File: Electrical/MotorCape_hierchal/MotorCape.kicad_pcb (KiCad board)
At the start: 2 copper layers, 24 parts, among them J1 FL, J10 T_SIG, J11 flag_wheel servo, J12 T_DB, J13 FR, J14 RightMotorController_PWR, J16 R_SIG, J17 BR, J2 LeftMotorController_PWR, J4 L_SIG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

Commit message: trying to lay-out things. lots of via's, this could be a bit messy
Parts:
- B1: value Front_Shifter -> SPARKFUN_LOGIC_LEVEL_CONVERTER
- B2: value Top_Shifter -> SPARKFUN_LOGIC_LEVEL_CONVERTER
- B3: value Right_Shifter -> SPARKFUN_LOGIC_LEVEL_CONVERTER
- J1: value FL -> Motor1
- J10: value T_SIG -> DualMotorController_SIG
- J12: value T_DB -> Motor2
- J13: value FR -> Motor1
- J14: value RightMotorController_PWR -> DualMotorController_PWR
- J16: value R_SIG -> DualMotorController_SIG
- J17: value BR -> Motor2
- J2: value LeftMotorController_PWR -> DualMotorController_PWR
- J4: value L_SIG -> DualMotorController_SIG
- J5: value BL -> Motor2
- J6: value T_FW -> Motor1
- J8: value TopMotorController_PWR -> DualMotorController_PWR
- P13: value batt_conn -> battery_connector
- moved J6 52.4 mm to (120.7, 88.3), turned to 180 degrees
- moved F1 37.8 mm to (123.9, 106.0)
- moved J12 33.3 mm to (119.6, 120.8), turned to 180 degrees
- moved U1 31.4 mm to (149.9, 101.0), turned to 180 degrees
- moved P13 29.2 mm to (70.5, 116.8), turned to 90 degrees
- moved P14 17.1 mm to (126.4, 101.6), turned to 180 degrees
- moved J14 16.2 mm to (83.2, 98.4)
- moved J2 15.0 mm to (108.6, 92.1)
- moved R1 12.5 mm to (144.2, 87.3), turned to 90 degrees
- moved J8 11.4 mm to (75.6, 72.4)
- moved R2 10.5 mm to (136.5, 84.5)
- moved J13 2.54 mm to (154.9, 108.0)
- moved J17 2.54 mm to (172.7, 108.6)
- moved J16 1.91 mm to (184.8, 114.3)
- moved J10 1.69 mm to (138.0, 110.7)
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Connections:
- J1 pad 2: Net-(J1-Pad2) -> MOTOR_GND
- J12 pad 2: Net-(J12-Pad2) -> MOTOR_GND
- J13 pad 2: Net-(J13-Pad2) -> MOTOR_GND
- J14 pad 1: Net-(J13-Pad2) -> MOTOR_GND
- J14 pad 6: Net-(J14-Pad6) -> MOTOR_GND
- J17 pad 2: Net-(J14-Pad6) -> MOTOR_GND
- J2 pad 1: Net-(J1-Pad2) -> MOTOR_GND
- J2 pad 6: Net-(J2-Pad6) -> MOTOR_GND
- J5 pad 2: Net-(J2-Pad6) -> MOTOR_GND
- J6 pad 2: Net-(J6-Pad2) -> MOTOR_GND
- J8 pad 1: Net-(J6-Pad2) -> MOTOR_GND
- J8 pad 6: Net-(J12-Pad2) -> MOTOR_GND
- R1 pad 2: Net-(R1-Pad2) -> +3V3
- R2 pad 1: SCL -> +3V3
- R2 pad 2: Net-(R2-Pad2) -> SCL
- U1 pad 12: Net-(R1-Pad2) -> SDA
- U1 pad 13: Net-(R2-Pad2) -> SCL
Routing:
- net +5V: track 0.00 -> 277.0 mm, vias 0 -> 2
- net Net-(J13-Pad1): track 0.00 -> 125.7 mm
- net +12V: track 0.00 -> 116.4 mm
- net Net-(J2-Pad5): track 0.00 -> 103.2 mm
- net Tx_To_Pi: track 0.00 -> 87.7 mm
- net Rx_From_Pi: track 0.00 -> 86.1 mm, vias 0 -> 1
- net MOTOR_PWR: track 0.00 -> 83.6 mm
- net +3V3: track 0.00 -> 77.9 mm, vias 0 -> 2
- net Net-(J14-Pad5): track 0.00 -> 74.4 mm
- net Net-(J1-Pad1): track 0.00 -> 67.9 mm
- net Net-(J12-Pad1): track 0.00 -> 54.2 mm
- net MOTOR_GND: track 0.00 -> 3.02 mm
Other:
- net class ArduinoSignals added: clearance 0.381, trace_width 0.381, via_dia 0.6858, via_drill 0.3302
- net class Default: clearance 0.2 -> 0.1524; trace_width 0.25 -> 0.1524; via_dia 0.6 -> 0.6858; via_drill 0.4 -> 0.3302
- net class IndvMotor added: clearance 1.016, trace_width 1.016, via_dia 0.6858, via_drill 0.3302
- net class MotorPower added: clearance 0.508, trace_width 2.032, via_dia 0.6858, via_drill 0.3302
- net class Signal added: clearance 0.381, trace_width 0.381, via_dia 0.6858, via_drill 0.3302
- net class SmallPower added: clearance 0.762, trace_width 0.762, via_dia 0.6858, via_drill 0.3302
- rule trace_clearance: 0.2 -> 0.1524
- rule trace_min: 0.2 -> 0.1524
- rule via_min_drill: 0.3 -> 0.3302
- rule via_min_size: 0.4 -> 0.6858
- board text added: "FR"
- board text added: "I2C"
- board text added: "Left"
- board text added: "Right"
- board text added: "Top"

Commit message: pushing changes while routing. still not done yet
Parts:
- moved J16 0.84 mm to (183.9, 114.2)
- moved B1 0.63 mm to (192.4, 111.8)
- moved B2 0.63 mm to (192.4, 97.8)
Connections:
- ARD1 pad 54: FrontLeft_ENC_A -> Net-(ARD1-Pad54)
- ARD1 pad 55: FrontLeft_ENC_B -> FrontLeft_ENC_A
- ARD1 pad 56: BackLeft_DIR -> Net-(ARD1-Pad56)
- ARD1 pad 57: BackLeft_ENC_A -> FrontLeft_ENC_B
- ARD1 pad 58: BackLeft_ENC_B -> Net-(ARD1-Pad58)
- ARD1 pad 59: FrontRight_DIR -> BackLeft_DIR
- ARD1 pad 60: FrontRight_ENC_A -> Net-(ARD1-Pad60)
- ARD1 pad 61: FrontRight_ENC_B -> BackLeft_ENC_A
- ARD1 pad 62: BackRight_DIR -> Net-(ARD1-Pad62)
- ARD1 pad 63: BackRight_ENC_A -> BackLeft_ENC_B
- ARD1 pad 64: BackRight_ENC_B -> Net-(ARD1-Pad64)
- ARD1 pad 65: FlagWheel_DIR -> FrontRight_DIR
- ARD1 pad 66: FlagWheel_ENC_A -> Net-(ARD1-Pad66)
- ARD1 pad 67: FlagWheel_ENC_B -> FrontRight_ENC_A
- ARD1 pad 68: DrawBridge_DIR -> Net-(ARD1-Pad68)
- ARD1 pad 69: DrawBridge_ENC_A -> FrontRight_ENC_B
- ARD1 pad 70: DrawBridge_ENC_B -> Net-(ARD1-Pad70)
- ARD1 pad 71: Net-(ARD1-Pad71) -> BackRight_DIR
- ARD1 pad 73: Net-(ARD1-Pad73) -> BackRight_ENC_A
- ARD1 pad 75: Net-(ARD1-Pad75) -> BackRight_ENC_B
- ARD1 pad 77: Net-(ARD1-Pad77) -> FlagWheel_DIR
- ARD1 pad 79: Net-(ARD1-Pad79) -> FlagWheel_ENC_A
- ARD1 pad 81: Net-(ARD1-Pad81) -> FlagWheel_ENC_B
- ARD1 pad 82: Net-(ARD1-Pad82) -> DrawBridge_DIR
- ARD1 pad 83: Net-(ARD1-Pad83) -> DrawBridge_ENC_A
- ARD1 pad 84: Net-(ARD1-Pad84) -> DrawBridge_ENC_B
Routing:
- net +3V3: track 77.9 -> 221.4 mm, vias 2 -> 9
- net Net-(J6-Pad1): track 0.00 -> 47.6 mm, vias 0 -> 1
- net Tx_To_Pi: track 87.7 -> 52.8 mm
- net Rx_From_Pi: track 86.1 -> 56.2 mm, vias 1 -> 0
- net DrawBridge_ENC_A: track 0.00 -> 29.1 mm, vias 0 -> 4
- net BackRight_DIR: track 0.00 -> 28.1 mm, vias 0 -> 3
- net BackRight_ENC_B: track 0.00 -> 17.6 mm, vias 0 -> 2
- net FlagWheel_DIR: track 0.00 -> 9.54 mm
- net FlagWheel_ENC_A: track 0.00 -> 7.47 mm, vias 0 -> 2
- net FrontRight_ENC_B: track 0.00 -> 6.81 mm, vias 0 -> 1
- net FlagWheel_ENC_B: track 0.00 -> 6.33 mm, vias 0 -> 2
- net BackRight_ENC_A: track 0.00 -> 4.88 mm, vias 0 -> 1
- net Net-(J13-Pad1): track 125.7 -> 130.4 mm, vias 0 -> 3
- net +5V: track 277.0 -> 278.4 mm, vias 2 -> 3
- added copper zone on B.Cu, net MOTOR_GND
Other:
- board outline added: 147.8 x 58.3 mm

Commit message: pushing latest motor controller layout changes
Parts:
- removed B1, B2, B3: SPARKFUN_LOGIC_LEVEL_CONVERTER, Sparkfun_Boards:SPARKFUN_LOGIC_LEVEL_CONVERTER
- removed J1, J13, J6: Motor1, MotorCapeComponents:Pin_Header_Latched_1x06
- removed J10, J16, J4: DualMotorController_SIG, MotorCapeComponents:Pin_Header_Latched_1x05
- removed J11: flag_wheel servo, MotorCapeComponents:Pin_Header_Latched_1x03
- removed J12, J17, J5: Motor2, MotorCapeComponents:Pin_Header_Latched_1x06
- removed J14, J2, J8: DualMotorController_PWR, Connectors_Phoenix:PhoenixContact_MSTBA-G_06x5.08mm_Angled
- removed J7: i2c bus connector, MotorCapeComponents:Pin_Header_Latched_1x02
- removed P14: Pi_Connector, MotorCapeComponents:Pin_Header_Latched_1x04
- added BL1: Motor2, MotorCapeComponents:Pin_Header_Latched_1x06, F.Cu at (135.2, 83.4)
- added BR1: Motor2, MotorCapeComponents:Pin_Header_Latched_1x06, F.Cu at (147.4, 115.3)
- added DrawBridge1: Motor2, MotorCapeComponents:Pin_Header_Latched_1x06, F.Cu at (128.3, 114.1)
- added FL1: Motor1, MotorCapeComponents:Pin_Header_Latched_1x06, F.Cu at (154.5, 80.8)
- added FR1: Motor1, MotorCapeComponents:Pin_Header_Latched_1x06, F.Cu at (147.4, 108.1)
- added FlagWheel1: Motor1, MotorCapeComponents:Pin_Header_Latched_1x06, F.Cu at (142.4, 102.0)
- added Left_PWR1: DualMotorController_PWR, Connectors_Phoenix:PhoenixContact_MSTBA-G_06x5.08mm_Angled, F.Cu at (96.4, 83.4)
- added Left_SIG1: DualMotorController_SIG, MotorCapeComponents:Pin_Header_Latched_1x05, F.Cu at (144.6, 93.4)
- added Left_Shifters1: SPARKFUN_LOGIC_LEVEL_CONVERTER, Sparkfun_Boards:SPARKFUN_LOGIC_LEVEL_CONVERTER, F.Cu at (180.5, 79.6)
- added Pi_Bus1: Pi_Connector, MotorCapeComponents:Pin_Header_Latched_1x04, F.Cu at (134.2, 85.4)
- added Right_PWR1: DualMotorController_PWR, Connectors_Phoenix:PhoenixContact_MSTBA-G_06x5.08mm_Angled, F.Cu at (97.9, 103.8)
- added Right_SIG1: DualMotorController_SIG, MotorCapeComponents:Pin_Header_Latched_1x05, F.Cu at (159.9, 93.8)
- added Right_Shifters1: SPARKFUN_LOGIC_LEVEL_CONVERTER, Sparkfun_Boards:SPARKFUN_LOGIC_LEVEL_CONVERTER, F.Cu at (180.4, 107.8)
- added Top_PWR1: DualMotorController_PWR, Connectors_Phoenix:PhoenixContact_MSTBA-G_06x5.08mm_Angled, F.Cu at (63.0, 81.8)
- added Top_SIG1: DualMotorController_SIG, MotorCapeComponents:Pin_Header_Latched_1x05, F.Cu at (134.5, 102.6)
- added Top_Shifters1: SPARKFUN_LOGIC_LEVEL_CONVERTER, Sparkfun_Boards:SPARKFUN_LOGIC_LEVEL_CONVERTER, F.Cu at (180.6, 93.7)
- added servo1: flag_wheel servo, MotorCapeComponents:Pin_Header_Latched_1x03, F.Cu at (105.0, 74.4)
- moved U1 51.7 mm to (103.5, 78.0), turned to 0 degrees
- moved R1 32.8 mm to (111.7, 92.0), turned to 0 degrees
- moved F1 29.6 mm to (97.6, 92.4), turned to 180 degrees
- moved R2 28.0 mm to (109.0, 89.5), turned to 270 degrees
- moved P13 17.4 mm to (83.6, 105.4), turned to 180 degrees
- moved ARD1 8.45 mm to (101.4, 66.8)
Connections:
- ARD1 pad 67: FrontRight_ENC_A -> FlagWheel_DIR
- ARD1 pad 69: FrontRight_ENC_B -> FlagWheel_ENC_A
- ARD1 pad 71: BackRight_DIR -> FlagWheel_ENC_B
- ARD1 pad 73: BackRight_ENC_A -> DrawBridge_DIR
- ARD1 pad 75: BackRight_ENC_B -> DrawBridge_ENC_A
- ARD1 pad 77: FlagWheel_DIR -> DrawBridge_ENC_B
- ARD1 pad 79: FlagWheel_ENC_A -> FrontRight_ENC_A
- ARD1 pad 81: FlagWheel_ENC_B -> FrontRight_ENC_B
- ARD1 pad 82: DrawBridge_DIR -> BackRight_DIR
- ARD1 pad 83: DrawBridge_ENC_A -> BackRight_ENC_A
- ARD1 pad 84: DrawBridge_ENC_B -> BackRight_ENC_B
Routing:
- net Net-(J13-Pad1): track 130.4 -> 0.00 mm, vias 3 -> 0
- net FlagWheel_DIR: track 9.54 -> 116.8 mm, vias 0 -> 7
- net Net-(J2-Pad5): track 103.2 -> 0.00 mm
- net +12V: track 116.4 -> 21.6 mm
- net Net-(FlagWheel1-Pad1): track 0.00 -> 90.0 mm, vias 0 -> 1
- net DrawBridge_DIR: track 0.00 -> 79.2 mm, vias 0 -> 15
- net Net-(FL1-Pad1): track 0.00 -> 75.5 mm, vias 0 -> 3
- net Net-(DrawBridge1-Pad1): track 0.00 -> 75.0 mm
- net Net-(J14-Pad5): track 74.4 -> 0.00 mm
- net Net-(BL1-Pad1): track 0.00 -> 73.3 mm
- net Net-(J1-Pad1): track 67.9 -> 0.00 mm
- net +5V: track 278.4 -> 212.7 mm, vias 3 -> 10
- net FrontLeft_DIR: track 0.00 -> 61.8 mm, vias 0 -> 6
- net +3V3: track 221.4 -> 159.8 mm, vias 9 -> 5
- net FrontRight_SPD: track 0.00 -> 58.3 mm, vias 0 -> 6
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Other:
- board size 147.8 x 58.3 mm -> 171.5 x 63.5 mm
- board text removed: "FR"
- board text removed: "I2C"
- board text removed: "Left"
- board text removed: "Right"
- board text removed: "Top"

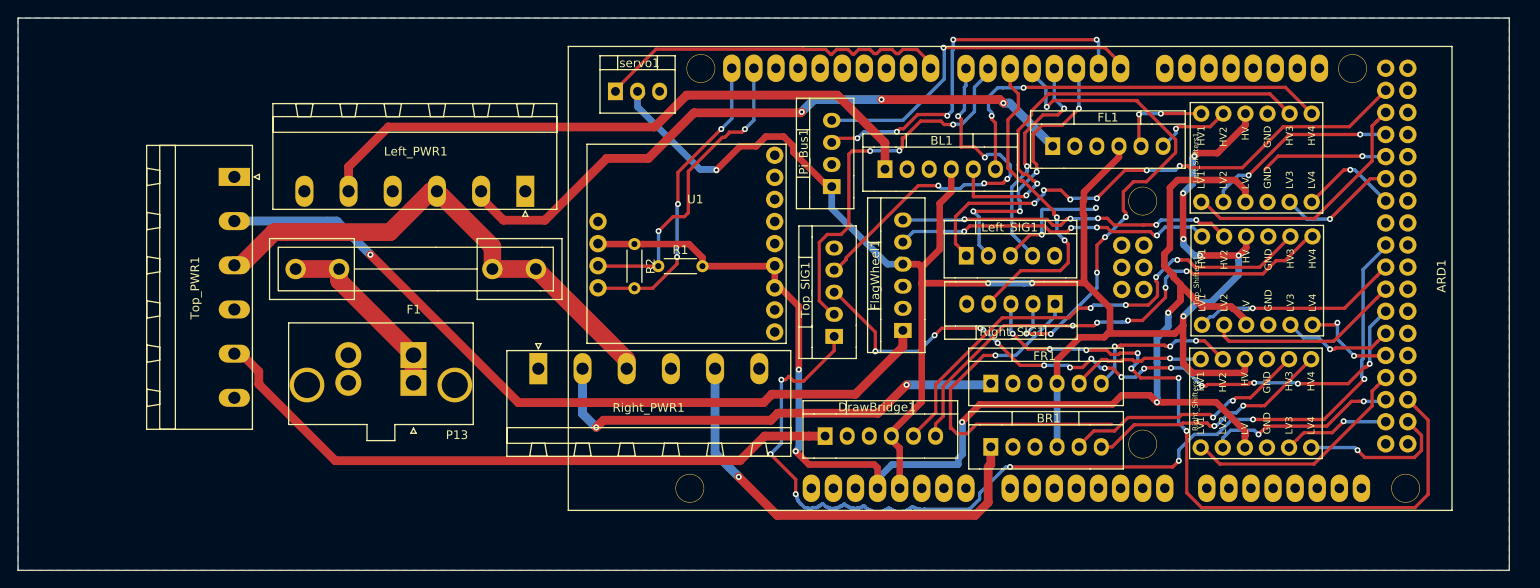
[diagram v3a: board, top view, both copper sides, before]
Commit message: finished the hierarchicalalala motor cape board
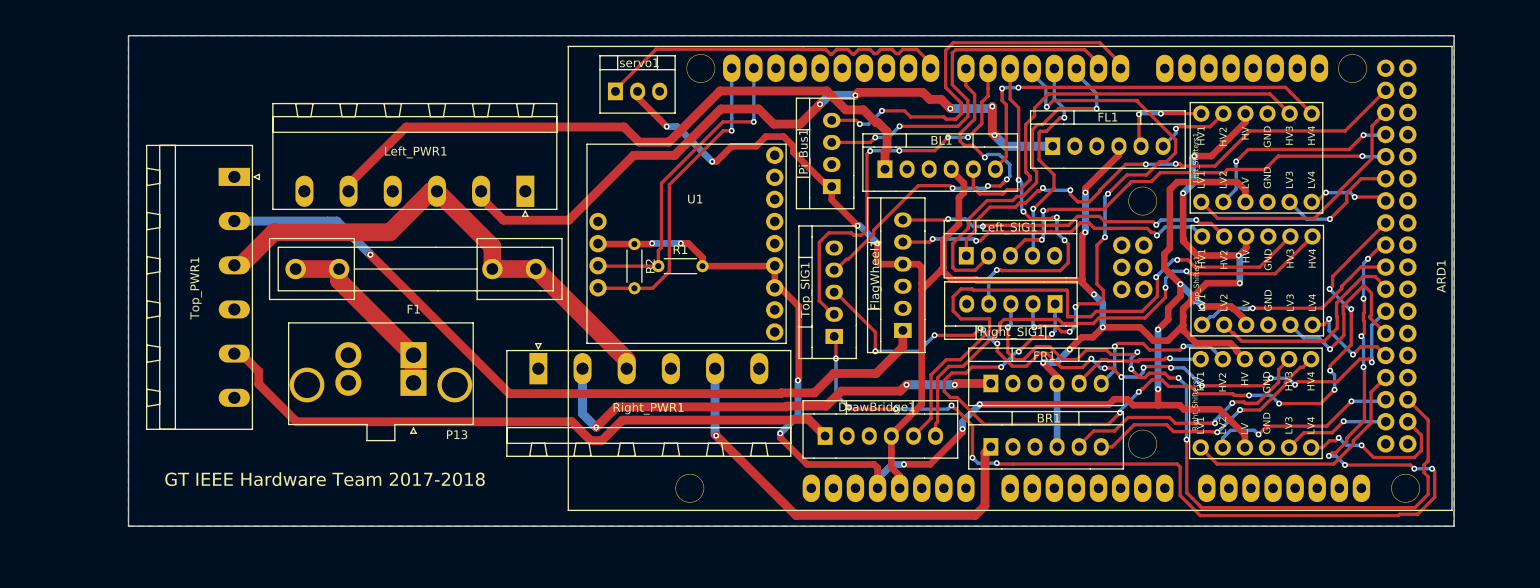
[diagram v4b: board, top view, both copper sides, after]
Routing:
- net FrontRight_DIR: track 40.7 -> 94.1 mm, vias 1 -> 11
- net BackLeft_DIR: track 28.4 -> 49.9 mm
- net Net-(DrawBridge1-Pad5): track 57.0 -> 72.4 mm, vias 4 -> 2
- net FlagWheel_DIR: track 116.8 -> 130.5 mm, vias 7 -> 14
- net FrontLeft_SPD: track 32.7 -> 42.0 mm, vias 4 -> 1
- net DrawBridge_ENC_A: track 12.9 -> 21.4 mm
- net Rx_From_Pi: track 40.2 -> 46.4 mm, vias 1 -> 2
- net BackRight_DIR: track 81.4 -> 86.9 mm, vias 7 -> 5
- net Net-(FL1-Pad1): track 75.5 -> 79.8 mm, vias 3 -> 5
- net Net-(BL1-Pad5): track 53.0 -> 49.6 mm, vias 2 -> 0
- net DrawBridge_DIR: track 79.2 -> 82.2 mm, vias 15 -> 13
- net BackRight_SPD: track 37.4 -> 40.1 mm, vias 2 -> 5
- net FlagWheel_ENC_B: track 22.6 -> 25.0 mm
- net BackLeft_ENC_B: track 11.5 -> 9.35 mm, vias 1 -> 2
- net FrontLeft_DIR: track 61.8 -> 59.7 mm, vias 6 -> 4
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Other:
- board size 171.5 x 63.5 mm -> 152.4 x 56.4 mm
- net class IndvMotor: clearance 1.016 -> 0.508
- net class SmallPower: clearance 0.762 -> 0.508
- board text added: "GT IEEE Hardware Team 2017-2018"
